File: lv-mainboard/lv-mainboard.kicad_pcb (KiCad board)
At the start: 2 copper layers, 190 x 120 mm, 110 parts, among them J1 Conn_02x13_Odd_Even, J12 CAN, J13 CAN_Brake, J14 CAN_lvbms, J15 CAN, J16 SideBoard, J17 SideBoard, J18 SideBoard, J19 SideBoard, J2 Conn_02x10_Odd_Even, J20 SideBoard, J21 SideBoard, J22 SDC OUT, J23 SDC OUT, J24 Mainhoop-Light, J25 ACC, J26 ACC, J27 ACC_PWR, J28 ACC_PRW, J3 Conn_02x10_Odd_Even, J30 BSE, J31 Brake Light, J32 Brake Light, J33 BSE, J34 Power, J35 Power, J4 Conn_02x10_Odd_Even, J7 FUNC1_LED, P7 Power, P8 Power, P9 Power, U1 AP63200WU, U2 AP63200WU

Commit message: feat: lv-mainboard v2025.12
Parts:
- removed E3: Power, Connector_JST:JST_XH_S2B-XH-A-1_1x02_P2.50mm_Horizontal
- removed the J7 at (65.0, 127.5)
- removed kibuzzard-6936E55A: G***, kibuzzard-6936E55A
- added C13: 1u, Capacitor_SMD:C_0603_1608Metric, B.Cu at (66.2, 88.5)
- added C14: 10u, Capacitor_SMD:C_0805_2012Metric, B.Cu at (62.5, 85.8)
- added J29: ACC, Connector_JST:JST_XH_B4B-XH-A_1x04_P2.50mm_Vertical, F.Cu at (165.0, 42.8)
- added J36: 1-Temp1, Connector_JST:JST_XH_B3B-XH-A_1x03_P2.50mm_Vertical, F.Cu at (56.5, 70.5)
- added J37: 1-Temp2, Connector_JST:JST_XH_B3B-XH-A_1x03_P2.50mm_Vertical, F.Cu at (56.5, 82.0)
- added J38: 1-PUMP, Connector_JST:JST_XH_B3B-XH-A_1x03_P2.50mm_Vertical, F.Cu at (56.5, 47.5)
- added J39: 1-FAN, Connector_JST:JST_XH_B3B-XH-A_1x03_P2.50mm_Vertical, F.Cu at (56.5, 59.0)
- added J40: 1-Pressure, Connector_JST:JST_XH_B3B-XH-A_1x03_P2.50mm_Vertical, F.Cu at (65.0, 82.0)
- added J41: 1-Flow, Connector_JST:JST_XH_B3B-XH-A_1x03_P2.50mm_Vertical, F.Cu at (65.0, 70.5)
- added J42: 2-Temp1, Connector_JST:JST_XH_B3B-XH-A_1x03_P2.50mm_Vertical, F.Cu at (56.5, 122.5)
- added J43: 2-Temp2, Connector_JST:JST_XH_B3B-XH-A_1x03_P2.50mm_Vertical, F.Cu at (56.5, 134.0)
- added J44: 2-Pressure, Connector_JST:JST_XH_B3B-XH-A_1x03_P2.50mm_Vertical, F.Cu at (65.0, 134.0)
- added J45: 2-Flow, Connector_JST:JST_XH_B3B-XH-A_1x03_P2.50mm_Vertical, F.Cu at (65.0, 122.5)
- added J46: 2-PUMP, Connector_JST:JST_XH_B3B-XH-A_1x03_P2.50mm_Vertical, F.Cu at (56.5, 99.0)
- added J47: 2-FAN, Connector_JST:JST_XH_B3B-XH-A_1x03_P2.50mm_Vertical, F.Cu at (56.5, 110.5)
- added J48: ACC, Connector_JST:JST_XH_B2B-XH-A_1x02_P2.50mm_Vertical, F.Cu at (154.8, 42.8)
- added R16: 100k, Resistor_SMD:R_0603_1608Metric, B.Cu at (60.8, 91.2)
- added R17: 301k, Resistor_SMD:R_0603_1608Metric, B.Cu at (59.5, 88.5)
- added TP3: TestPoint, TestPoint:TestPoint_THTPad_D1.5mm_Drill0.7mm, F.Cu at (56.2, 87.8)
- added U3: AP2204K-ADJ, Package_TO_SOT_SMD:SOT-23-5, B.Cu at (62.8, 88.5)
- added kibuzzard-6945460C: G***, kibuzzard-6945460C, F.Cu at (193.5, 35.5)
- added kibuzzard-6945462F: G***, kibuzzard-6945462F, F.Cu at (230.8, 103.0)
- added kibuzzard-69454637: G***, kibuzzard-69454637, F.Cu at (236.8, 120.4)
- added kibuzzard-69454910: G***, kibuzzard-69454910, F.Cu at (146.5, 45.8)
- added kibuzzard-69454A4D: G***, kibuzzard-69454A4D, F.Cu at (109.0, 46.2)
- added kibuzzard-69454B20: G***, kibuzzard-69454B20, F.Cu at (68.5, 45.0)
- added kibuzzard-69454C2F: G***, kibuzzard-69454C2F, F.Cu at (68.5, 97.2)
- added kibuzzard-69455236: G***, kibuzzard-69455236, F.Cu at (199.8, 126.8)
- R14, R15: value R -> 150R
- moved J15 45.3 mm to (230.2, 118.4)
- moved J14 45.3 mm to (230.2, 126.9)
- moved J12 45.3 mm to (230.2, 143.1)
- moved J13 45.3 mm to (230.2, 135.0)
- moved D4 44.1 mm to (198.4, 117.1)
- moved F4 44.1 mm to (186.8, 117.7)
- moved R8 44.1 mm to (198.4, 117.5)
- moved J28 11.8 mm to (184.2, 142.5)
- moved H1 2.50 mm to (57.5, 34.0)
- moved H2 2.50 mm to (240.5, 34.0)
- moved H3 2.50 mm to (57.5, 142.0)
- moved H4 2.50 mm to (240.5, 142.0)
- moved J16 1.93 mm to (241.5, 82.2)
- moved J26 1.58 mm to (165.0, 33.5)
- moved J21 1.55 mm to (241.5, 64.8)
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- renumbered P8 to J10, P9 to J11, E2 to J5, E1 to J6, E1 to J7, E3 to J8, P7 to J9
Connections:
- J10 pad 1: P8 -> GND
- J10 pad 2: GND -> P8
- J11 pad 1: P9 -> GND
- J11 pad 2: GND -> P9
- J22 pad 2: GND -> SDC_OUT
- J23 pad 2: GND -> SDC_OUT
- J30 pad 1: GND -> P2
- J33 pad 1: GND -> P2
- J34 pad 1: P5 -> GND
- J34 pad 2: P6 -> P5
- J35 pad 1: P5 -> GND
- J35 pad 2: P6 -> P5
- J5 pad 1: E2 -> GND
- J5 pad 2: GND -> E2
- J6 pad 1: E1 -> GND
- J6 pad 2: GND -> E1
- J7 pad 1: E1 -> GND
- J7 pad 2: GND -> E1
- J8 pad 1: E3 -> GND
- J8 pad 2: GND -> E3
- J9 pad 1: P7 -> GND
- J9 pad 2: GND -> P7
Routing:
- net GND: track 10.6 -> 552.3 mm, vias 26 -> 135
- net CAN-: track 221.0 -> 500.5 mm
- net CAN+: track 223.3 -> 502.5 mm
- net E3: track 0.00 -> 253.5 mm
- net E1: track 0.07 -> 253.2 mm, vias 16 -> 2
- net E2: track 0.00 -> 155.3 mm
- net P4: track 0.00 -> 136.5 mm
- net +6V: track 18.2 -> 144.8 mm
- net TSAL: track 0.00 -> 114.1 mm, vias 0 -> 2
- net +5V: track 0.00 -> 110.2 mm
- net P2: track 0.00 -> 98.7 mm
- net BSE_L_Fault: track 0.00 -> 98.3 mm
- net BSE_R_Fault: track 0.00 -> 95.7 mm
- net BSPD_signal4: track 0.00 -> 94.9 mm
- net BSPD: track 0.00 -> 93.0 mm
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- added copper zone on B.Cu, net +6V
- added copper zone on F.Cu, net GND
- added copper zone on B.Cu, net Net-(U2-FB)
- added copper zone on B.Cu, net Net-(U2-SW)
- added copper zone on F.Cu, net SDC_OUT
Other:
- board size 190 x 120 mm -> 195 x 120 mm
- board text added: "15V"
- board text added: "6V"
- board text added: "BMS"
- board text added: "BSE_L"
- board text added: "BSE_R"
- board text added: "BSPD"
- board text added: "Brake"
- board text added: "Current"
- board text added: "DAQ1"
- board text added: "DAQ2"
- board text added: "E1"
- board text added: "E2"
- board text added: "E3"
- board text added: "FAN"
- board text added: "Flow"
- board text added: "IMD"
- board text added: "IN_ACC"
- board text added: "LED"
- board text added: "LV1"
- board text added: "LV11"
- board text added: "LV12"
- board text added: "LV13"
- board text added: "LV14"
- board text added: "LV2"
- board text added: "LV3"
- board text added: "LV5"
- board text added: "LV6"
- board text added: "LV7"
- board text added: "LV8"
- board text added: "LV9"
- board text added: "Lv_BMS"
- board text added: "OUT_Ctrl"
- board text added: "P1"
- board text added: "P2"
- board text added: "P3"
- board text added: "P4"
- board text added: "P5"
- board text added: "P6"
- board text added: "P7"
- board text added: "P8"
- board text added: "P9"
- board text added: "PUMP"
- board text added: "PWM"
- board text added: "Pressure"
- board text added: "RST"
- board text added: "SDC"
- board text added: "TSAL"
- board text added: "TSSI"
- board text added: "Temp1"
- board text added: "Temp2"
- board text added: "v2025.12"

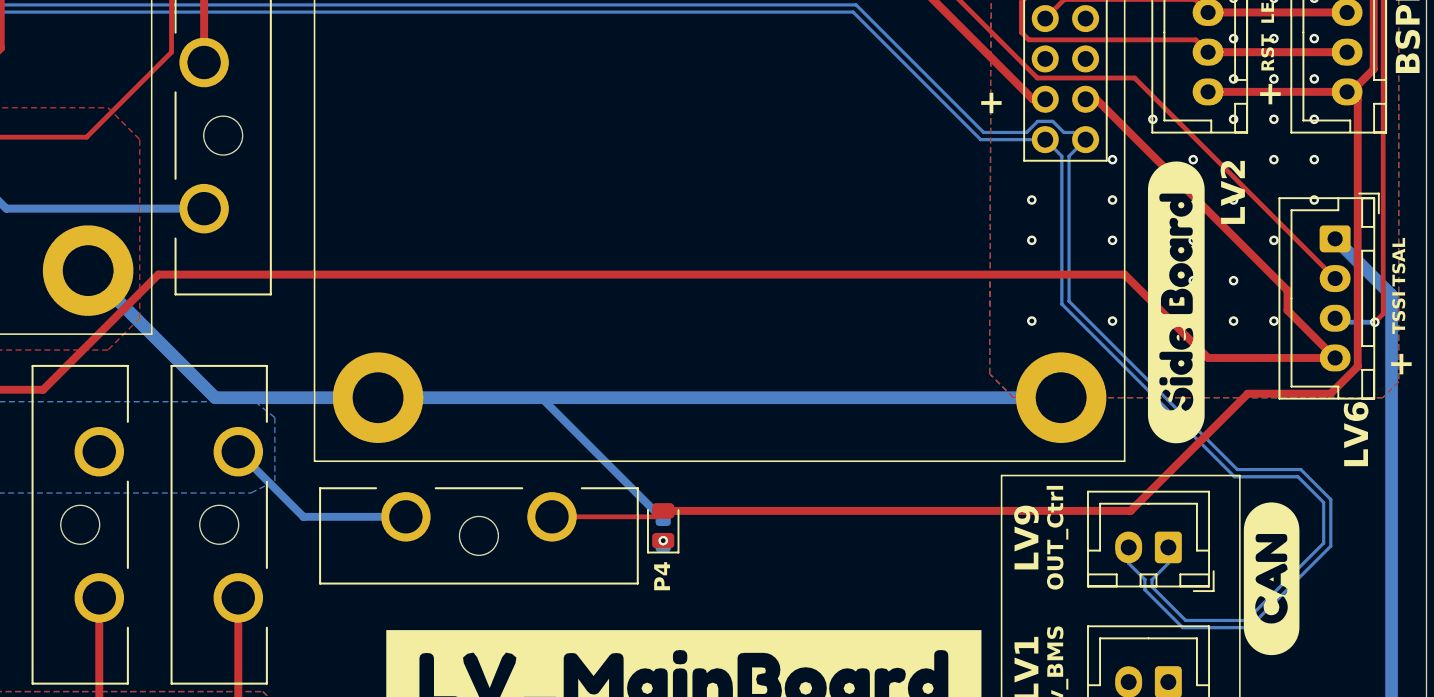
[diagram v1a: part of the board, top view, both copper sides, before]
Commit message: modify: replace SDC pwr with P8
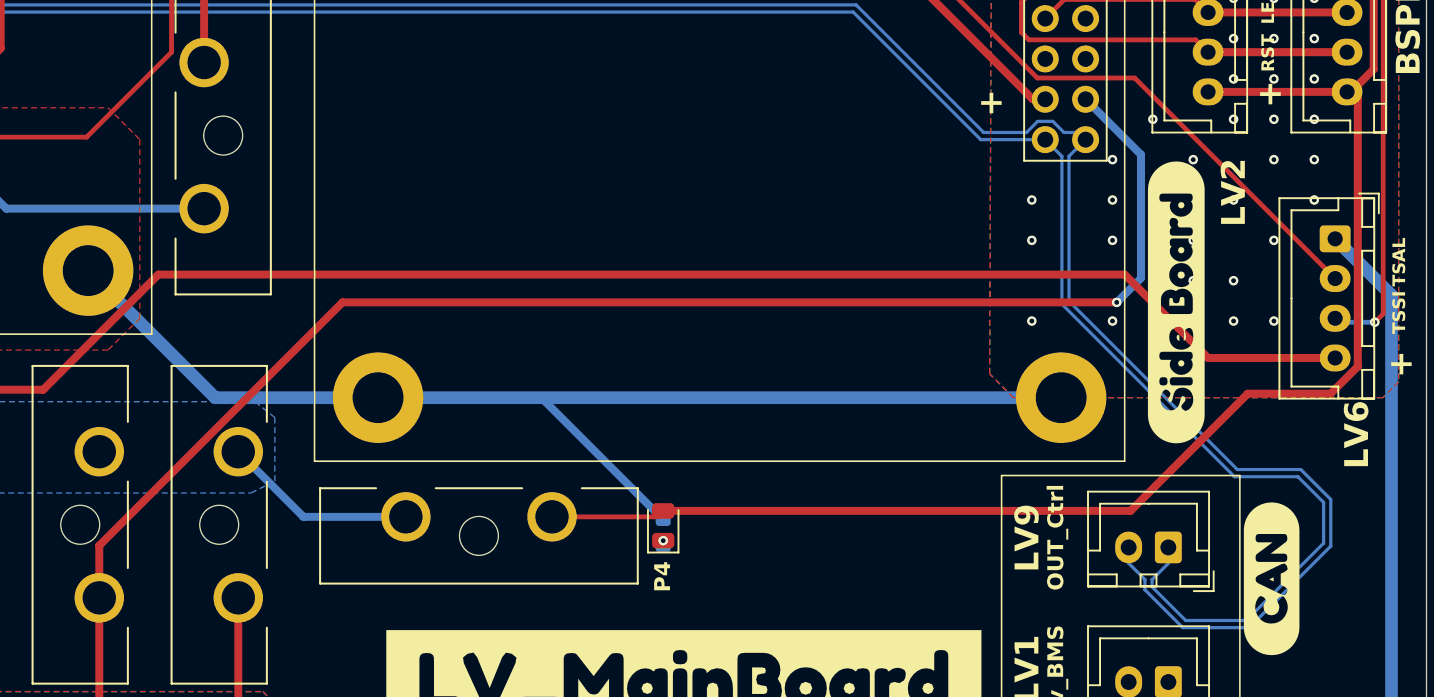
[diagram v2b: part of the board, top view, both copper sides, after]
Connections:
- J1 pad 23: E2 -> P8
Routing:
- net P8: track 14.5 -> 103.0 mm, vias 0 -> 1
- net E2: track 155.3 -> 132.1 mm
